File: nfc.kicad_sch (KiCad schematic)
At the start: 14 parts, among them U6 ST25DV64KC-JF6D3

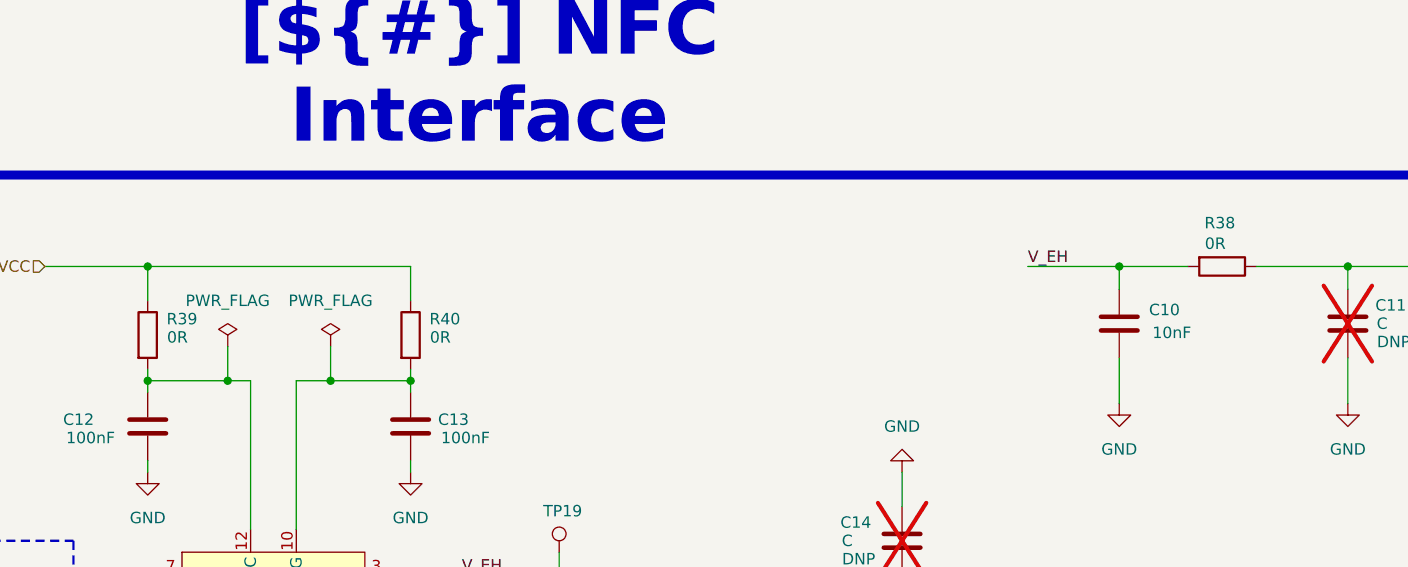
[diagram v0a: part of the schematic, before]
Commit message: fix(hardware): replace jumper/passive footprints with 0402 and refine schematics
- Replace 0-ohm jumper resistors with 0402 package equivalents
- Reduce package size on several capacitors
- Correct and simplify several schematic symbols (replaced with
  simplified equivalents where the original was overcomplicated)
- Bump lib submodule to the updated component library (renamed
  switch footprints, new Conn_01x02_MountingPin symbol, pad/pin
  numbering fixes, approved IPN assignments, Workart artwork library)
- Register Workart.pretty in fp-lib-table
- Mark J3 as DNP in mcu.kicad_sch
- Continue schematic wiring/placement (Leds.kicad_sch, tessera.kicad_sch)
  and PCB routing/placement (tessera.kicad_pcb)
- Add board outline source (Images/pcb_size.dxf, pcb_shape.FCStd) and
  silkscreen artwork sources (Logos/) for the Workart footprints
- Complete preliminary version of PCB
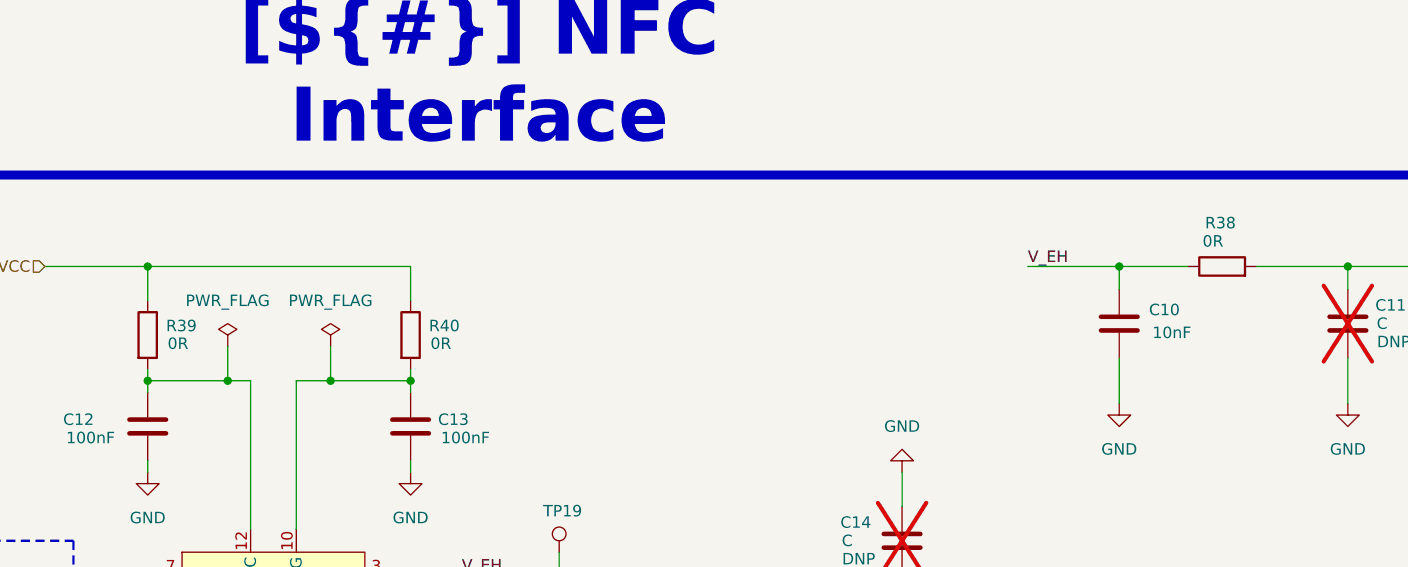
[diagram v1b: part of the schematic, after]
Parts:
- removed R38, R39, R40: 0R ±5% 1/10W, Resistor_SMD:R_0603_1608Metric, symbol catalog:Resistors/R0603_0R_0.1W_±5%
- added R38, R39, R40: 0R ±5% 1/16W, Resistor_SMD:R_0402_1005Metric, symbol catalog:Resistors/R0402_0R_0.1W_±5%
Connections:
- net VCC: now also R39.1, R40.1
- net VCC_EH: now also R38.2
- net V_EH: now also R38.1
- net at C13.1, U6.10 (VDCG): now also R40.2
- net at C12.1, U6.12 (VCC): now also R39.2

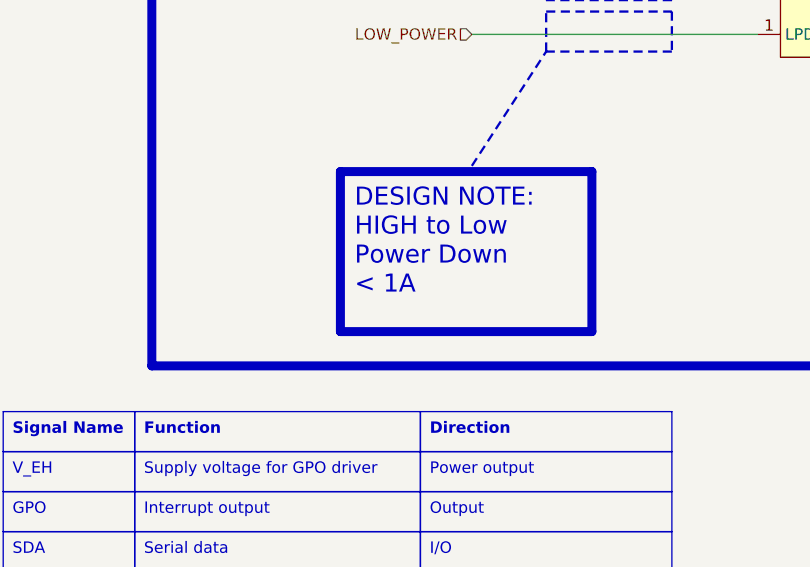
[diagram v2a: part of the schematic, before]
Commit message: fix(hardware): tighten PCB edge clearance and diff-pair rules, update logo
- Bump lib submodule: assign IPNs to another batch of approved
  capacitor selections
- Update the embedded logo artwork on every schematic sheet to the
  new Logos/logo.png
- Increase min_copper_edge_clearance to 0.5mm and raise net class
  clearance/spacing to match
- Replace the generic outer/inner-layer trace width & spacing rules
  with a dedicated "USB Diff Pair clearance to other nets" rule
  (0.2023mm, excluding intra-pair spacing already governed by the
  netclass diff_pair_gap)
- Add DRC exclusions for pre-existing clearance/copper-edge/solder-
  mask-bridge items surfaced by the tightened edge-clearance rule
- Continue schematic placement and PCB routing/placement
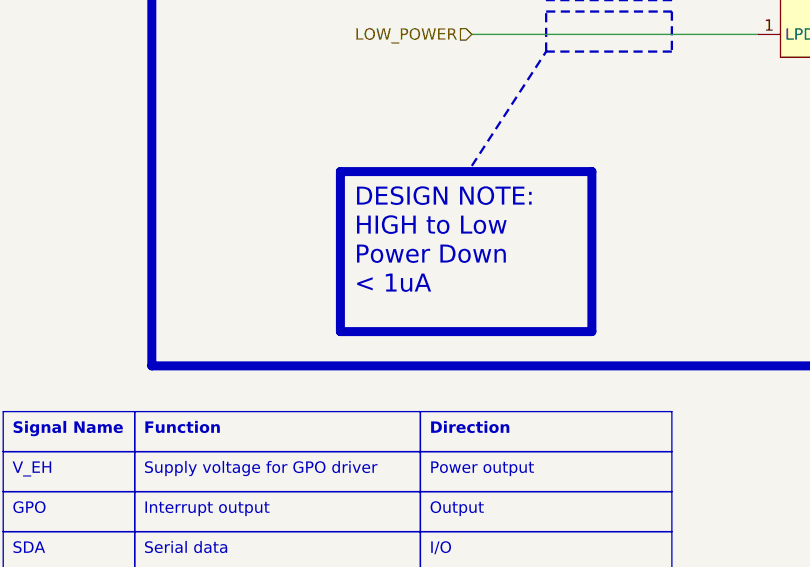
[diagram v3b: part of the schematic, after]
